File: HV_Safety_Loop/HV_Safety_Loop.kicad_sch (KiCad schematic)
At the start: 29 parts, among them J1 SL, J10 OUT5, J11 OUT6, J12 OUT7, J13 OUT8, J14 OUT9, J15 OUT10, J2 Filter_Cap, J3 Filter_Cap, J4 Filter_Cap, J5 PLC_EN, J6 OUT1, J7 OUT2, J8 OUT3, J9 OUT4

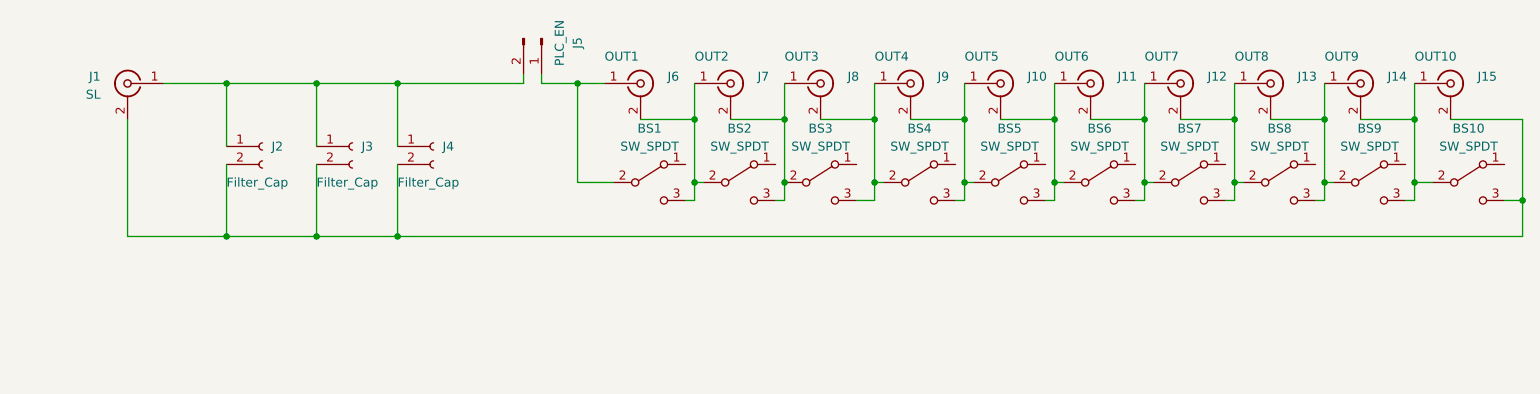
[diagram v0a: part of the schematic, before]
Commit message: change bypass switch to E1218, add bypass capacitor for plc connector
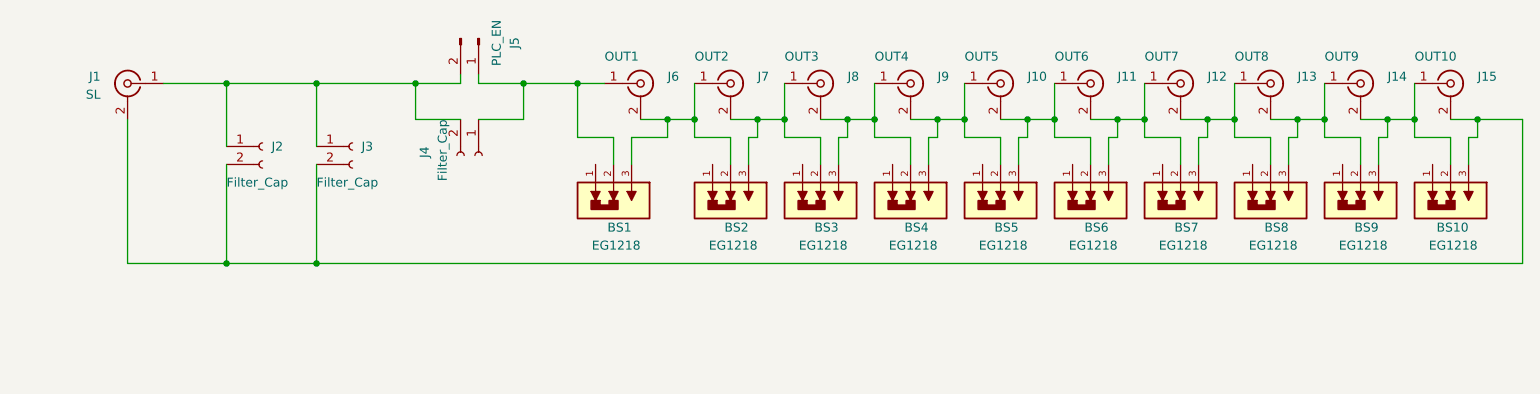
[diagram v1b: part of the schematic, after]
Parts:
- removed BS1, BS10, BS2, BS3, BS4, BS5, BS6, BS7, BS8, BS9: SW_SPDT, Button_Switch_THT:SW_E-Switch_EG1271_SPDT, symbol Switch:SW_SPDT
- added BS1, BS10, BS2, BS3, BS4, BS5, BS6, BS7, BS8, BS9: EG1218, footprints:SW_EG1218, symbol E1218:EG1218
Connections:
- net at J13.2 (Ext), J14.1 (In): now also BS8.3, BS9.2
- net at J14.2 (Ext), J15.1 (In): now also BS10.2, BS9.3
- net at J5.1 (Pin_1), J6.1 (In): now also J4.1 (Pin_1), BS1.2
- net at J6.2 (Ext), J7.1 (In): now also BS1.3, BS2.2
- net at J12.2 (Ext), J13.1 (In): now also BS7.3, BS8.2
- net at J7.2 (Ext), J8.1 (In): now also BS2.3, BS3.2
- net at J8.2 (Ext), J9.1 (In): now also BS3.3, BS4.2
- net at J1.1 (In), J2.1 (Pin_1), J3.1 (Pin_1)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: now also J4.2 (Pin_2); no longer J4.1 (Pin_1)
- net at J1.2 (Ext), J15.2 (Ext), J2.2 (Pin_2)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: now also BS10.3; no longer J4.2 (Pin_2)
- net at J11.2 (Ext), J12.1 (In): now also BS6.3, BS7.2
- net at J10.1 (In), J9.2 (Ext): now also BS4.3, BS5.2
- net at J10.2 (Ext), J11.1 (In): now also BS5.3, BS6.2
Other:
- moved on the sheet: J4, J5
